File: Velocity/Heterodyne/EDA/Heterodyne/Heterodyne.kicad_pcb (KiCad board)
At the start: 2 copper layers, 59 x 44 mm, 31 parts, among them J3 PWR, J4 Doppler_Out, J5 V_Square, J6 OP_OUT, J7 Reciever, J8 Emmiter, U1 SA612AD, U2 NE5532, U3 MAX7375AXR105

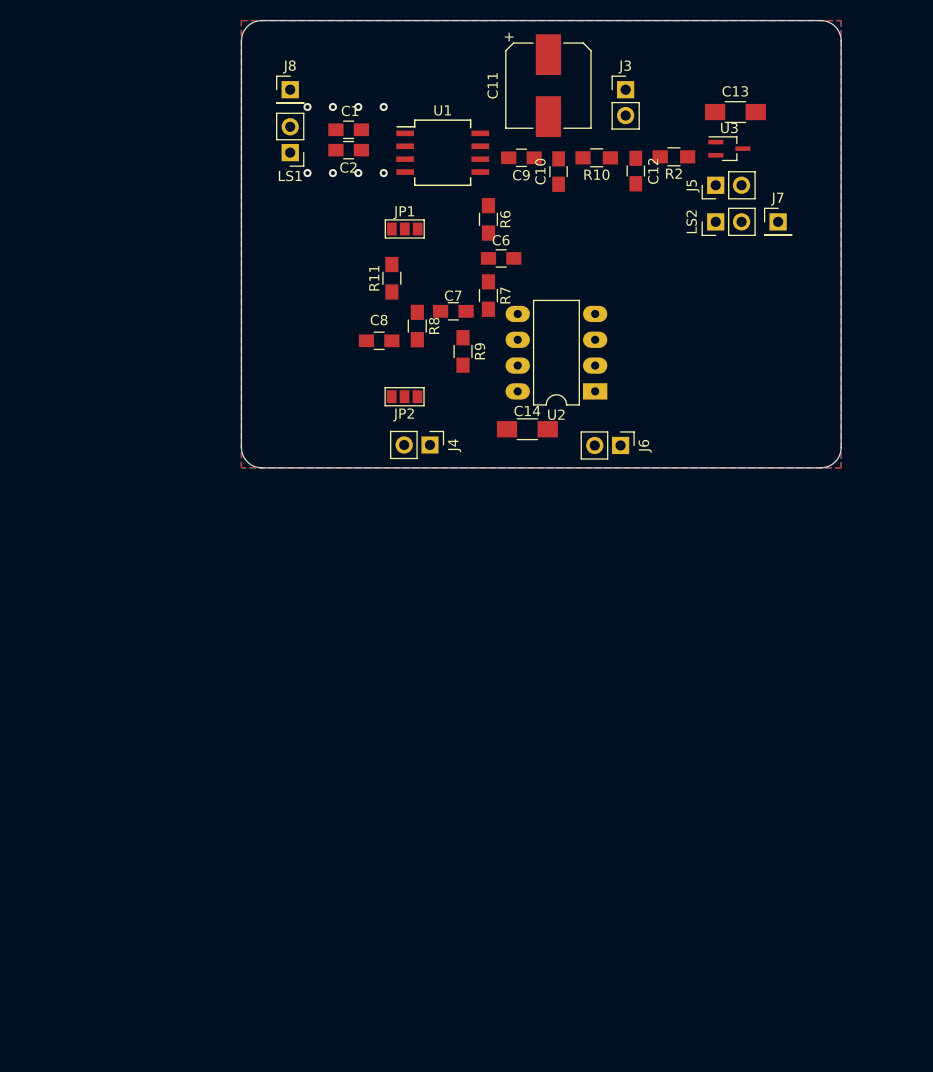
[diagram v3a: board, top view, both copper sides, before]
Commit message: updated data to heterodyne pcb to include adc
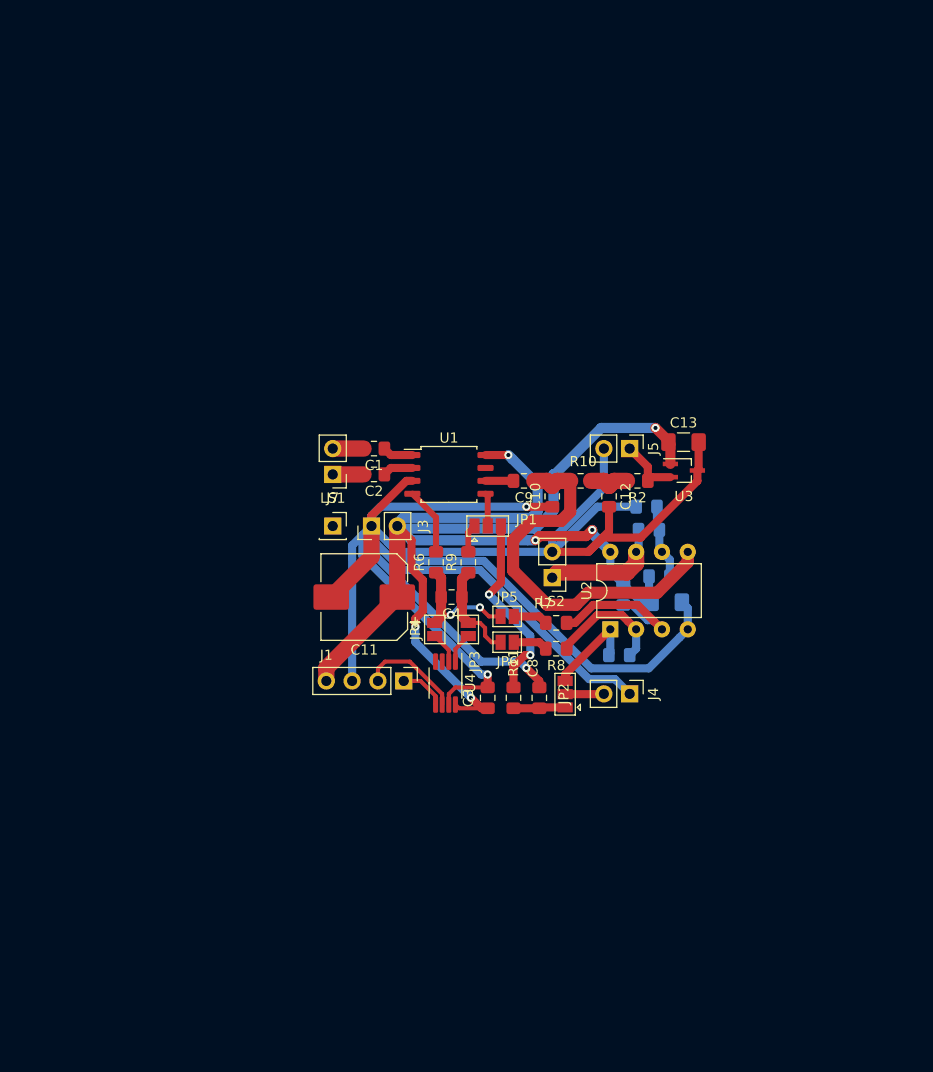
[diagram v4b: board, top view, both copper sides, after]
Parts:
- removed C6, C7: 100 nF, Capacitors_SMD:C_0805_HandSoldering
- removed J6: OP_OUT, Pin_Headers:Pin_Header_Straight_1x02_Pitch2.54mm
- removed J8: Emmiter, Pin_Headers:Pin_Header_Straight_1x01_Pitch2.54mm
- added C3: 100 nF, Capacitor_SMD:C_0805_2012Metric_Pad1.15x1.40mm_HandSolder, F.Cu at (149.2, 102.6)
- added C4: 22 nF, Capacitor_SMD:C_0805_2012Metric_Pad1.15x1.40mm_HandSolder, F.Cu at (145.7, 92.7)
- added J1: I2C, Connector_PinHeader_2.54mm:PinHeader_1x04_P2.54mm_Vertical, F.Cu at (141.0, 101.0)
- added JP3: SolderJumper_2_Open, Jumper:SolderJumper-2_P1.3mm_Open_Pad1.0x1.5mm, F.Cu at (147.3, 95.9)
- added JP4: SolderJumper_2_Open, Jumper:SolderJumper-2_P1.3mm_Open_Pad1.0x1.5mm, F.Cu at (144.0, 95.9)
- added JP5: SolderJumper_2_Open, Jumper:SolderJumper-2_P1.3mm_Open_Pad1.0x1.5mm, F.Cu at (151.1, 94.6)
- added JP6: SolderJumper_2_Open, Jumper:SolderJumper-2_P1.3mm_Open_Pad1.0x1.5mm, F.Cu at (151.1, 97.2)
- added R1: 1 kΩ, Resistor_SMD:R_0805_2012Metric_Pad1.15x1.40mm_HandSolder, B.Cu at (166.1, 90.7)
- added R12: 18 kΩ, Resistor_SMD:R_0805_2012Metric_Pad1.15x1.40mm_HandSolder, B.Cu at (162.2, 98.4)
- added R3: 1 kΩ, Resistor_SMD:R_0805_2012Metric_Pad1.15x1.40mm_HandSolder, B.Cu at (164.9, 83.8)
- added R4: 39 kΩ, Resistor_SMD:R_0805_2012Metric_Pad1.15x1.40mm_HandSolder, B.Cu at (165.1, 86.1)
- added R5: 18 kΩ, Resistor_SMD:R_0805_2012Metric_Pad1.15x1.40mm_HandSolder, B.Cu at (162.6, 92.5)
- added U4: MAX11613, Package_SO:MSOP-8_3x3mm_P0.65mm, F.Cu at (145.1, 101.2)
- C1, C10, C12, C2, C9: footprint Capacitors_SMD:C_0805_HandSoldering -> Capacitor_SMD:C_0805_2012Metric_Pad1.15x1.40mm_HandSolder
- C11: footprint Capacitors_SMD:CP_Elec_8x10 -> Capacitor_SMD:CP_Elec_8x10
- C13: footprint Capacitors_SMD:C_1206_HandSoldering -> Capacitor_SMD:C_1206_3216Metric_Pad1.42x1.75mm_HandSolder
- C14: footprint Capacitors_SMD:C_1206_HandSoldering -> Capacitor_SMD:C_1206_3216Metric_Pad1.42x1.75mm_HandSolder; moved to B.Cu
- C8: value 100 nF -> 22 nF; footprint Capacitors_SMD:C_0805_HandSoldering -> Capacitor_SMD:C_0805_2012Metric_Pad1.15x1.40mm_HandSolder
- J3, J4, J5, LS1, LS2: footprint Pin_Headers:Pin_Header_Straight_1x02_Pitch2.54mm -> Connector_PinHeader_2.54mm:PinHeader_1x02_P2.54mm_Vertical
- J7: footprint Pin_Headers:Pin_Header_Straight_1x01_Pitch2.54mm -> Connector_PinSocket_2.54mm:PinSocket_1x01_P2.54mm_Vertical
- JP1, JP2: footprint Connectors:GS3 -> Jumper:SolderJumper-3_P1.3mm_Open_Pad1.0x1.5mm
- R10, R11, R2: footprint Resistors_SMD:R_0805_HandSoldering -> Resistor_SMD:R_0805_2012Metric_Pad1.15x1.40mm_HandSolder
- R6: value 10 kΩ -> 330 Ω; footprint Resistors_SMD:R_0805_HandSoldering -> Resistor_SMD:R_0805_2012Metric_Pad1.15x1.40mm_HandSolder
- R7, R8: value 10 kΩ -> 1 kΩ; footprint Resistors_SMD:R_0805_HandSoldering -> Resistor_SMD:R_0805_2012Metric_Pad1.15x1.40mm_HandSolder
- R9: value 39 kΩ -> 330 Ω; footprint Resistors_SMD:R_0805_HandSoldering -> Resistor_SMD:R_0805_2012Metric_Pad1.15x1.40mm_HandSolder
- U1: footprint Housings_SOIC:SO-8_5.3x6.2mm_Pitch1.27mm -> Package_SO:SOIC-8_5.275x5.275mm_P1.27mm
- U2: footprint Housings_DIP:DIP-8_W7.62mm_LongPads -> Package_DIP:DIP-8_W7.62mm
- U3: footprint TO_SOT_Packages_SMD:SOT-323_SC-70_Handsoldering -> Package_TO_SOT_SMD:SOT-323_SC-70_Handsoldering
- moved C11 53.5 mm to (137.1, 92.7), turned to 180 degrees
- moved J7 53.1 mm to (134.0, 85.7)
- moved J3 49.7 mm to (137.8, 85.7), turned to 90 degrees
- moved R11 43.0 mm to (151.8, 102.6)
- moved LS2 38.5 mm to (155.6, 90.8), turned to 180 degrees
- moved C8 38.5 mm to (154.3, 102.6), turned to 90 degrees
- moved R8 34.6 mm to (156.0, 97.8), turned to 180 degrees
- moved R6 34.1 mm to (144.1, 89.3), turned to 90 degrees
- moved JP2 33.3 mm to (156.8, 102.3)
- moved R7 32.9 mm to (156.0, 95.2), turned to 180 degrees
- moved C13 32.9 mm to (168.5, 77.5)
- moved C12 32.1 mm to (161.2, 82.8)
- moved R2 32.1 mm to (164.0, 81.3)
- moved C2 32.0 mm to (138.0, 80.6)
- moved U3 32.0 mm to (168.5, 80.3)
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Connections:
- JP1 pad 1: Net-(C7-Pad2) -> Net-(JP1-Pad1)
- JP2 pad 3: Net-(C6-Pad2) -> Net-(JP2-Pad3)
- LS2 pad 1: Net-(J5-Pad1) -> Net-(LS2-Pad1)
- R6 pad 1: Net-(R6-Pad1) -> Net-(C4-Pad2)
- R6 pad 2: Net-(C6-Pad1) -> Net-(R6-Pad2)
- R7 pad 1: Net-(C6-Pad1) -> Net-(R5-Pad1)
- R7 pad 2: Net-(C7-Pad1) -> Net-(JP5-Pad2)
- R8 pad 1: Net-(C7-Pad2) -> Net-(R12-Pad1)
- R8 pad 2: Net-(R8-Pad2) -> Net-(JP6-Pad2)
- R9 pad 1: Net-(R8-Pad2) -> Net-(C4-Pad1)
- R9 pad 2: Net-(C6-Pad2) -> Net-(JP1-Pad1)
- U1 pad 4: Net-(JP1-Pad2) -> Net-(R6-Pad2)
- U1 pad 5: Net-(R6-Pad1) -> Net-(JP1-Pad2)
- U2 pad 1: Net-(J6-Pad2) -> Net-(JP2-Pad3)
- U2 pad 2: Net-(R1-Pad2) -> Net-(R12-Pad1)
- U2 pad 3: Driver_Wave -> Net-(R5-Pad1)
- U2 pad 5: Net-(C7-Pad1) -> Driver_Wave
- U2 pad 6: Net-(R8-Pad2) -> Net-(R1-Pad2)
- U2 pad 7: Net-(C6-Pad2) -> Net-(LS2-Pad1)
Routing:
- net GND: track 0.00 -> 240.8 mm, vias 8 -> 3
- net VPP: track 0.00 -> 136.4 mm, vias 0 -> 6
- net Driver_Wave: track 0.00 -> 38.1 mm
- net Net-(JP1-Pad3): track 0.00 -> 19.0 mm, vias 0 -> 2
- net Net-(R5-Pad1): track 0.00 -> 15.9 mm
- net Net-(LS2-Pad1): track 0.00 -> 12.2 mm
- net Net-(C4-Pad2): track 0.00 -> 12.0 mm, vias 0 -> 2
- net Net-(R12-Pad1): track 0.00 -> 11.8 mm
- net Net-(J1-Pad2): track 0.00 -> 10.2 mm
- net Net-(C4-Pad1): track 0.00 -> 9.87 mm
- net Net-(JP2-Pad3): track 0.00 -> 9.52 mm
- net Net-(R1-Pad2): track 0.00 -> 7.38 mm
- net Net-(R6-Pad2): track 0.00 -> 6.68 mm
- net Net-(J5-Pad1): track 0.00 -> 6.28 mm
- net Net-(C8-Pad1): track 0.00 -> 5.12 mm
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- removed copper zone on B.Cu, net GND
- removed copper zone on F.Cu, net GND
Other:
- board outline removed

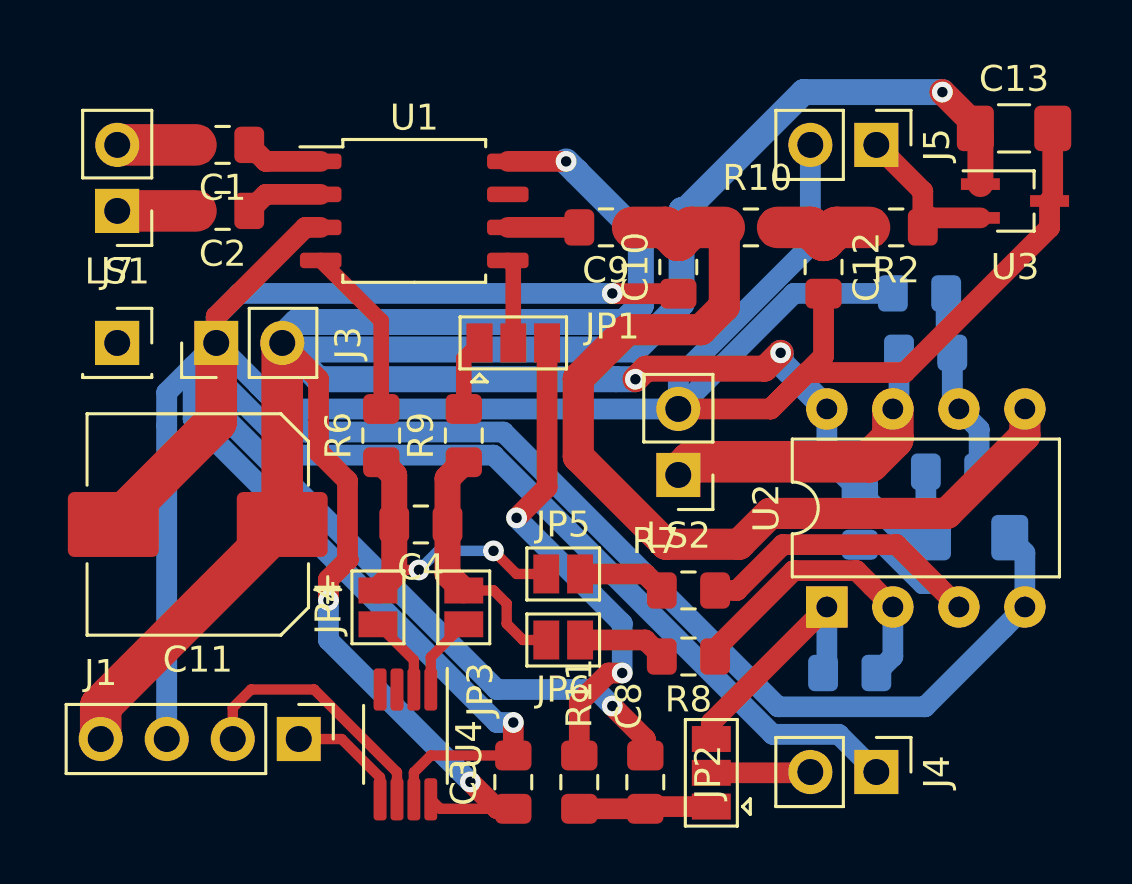
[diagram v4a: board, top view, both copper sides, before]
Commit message: finshsed routing 2 layer board
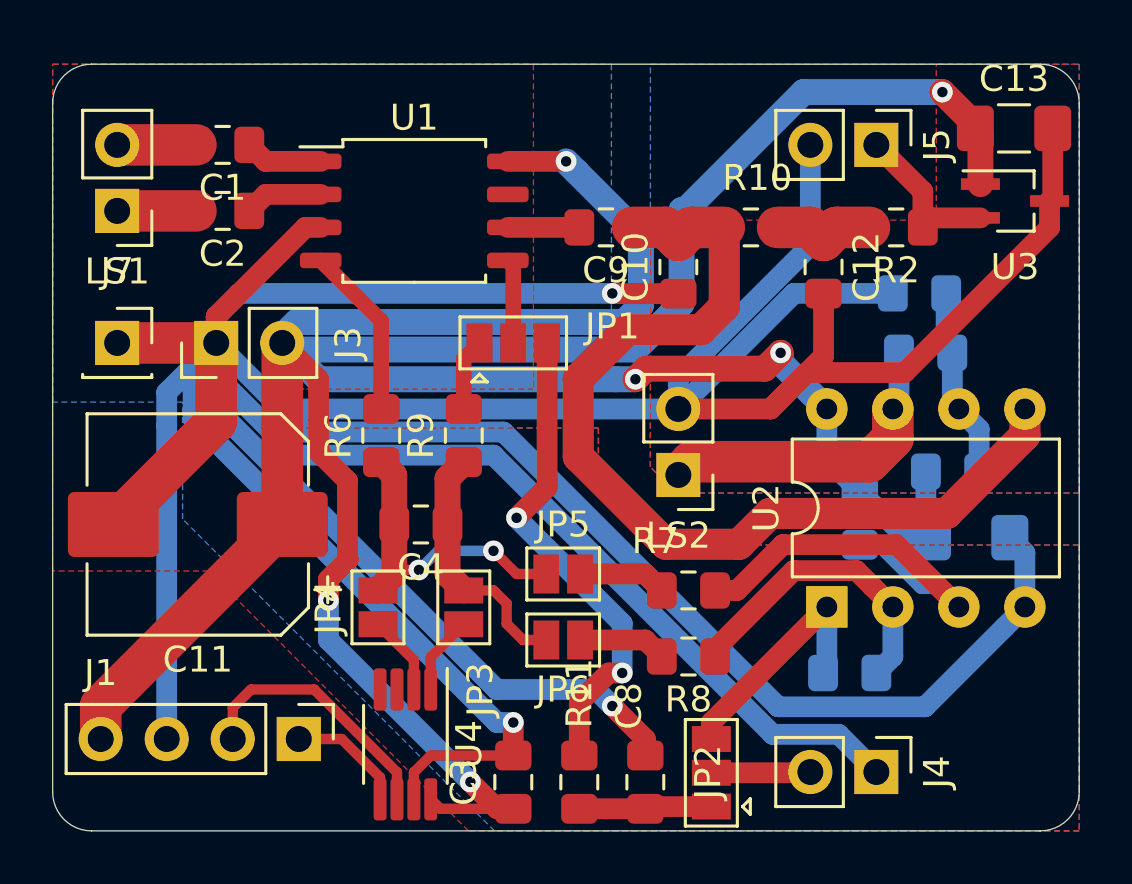
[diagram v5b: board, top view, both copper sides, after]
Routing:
- net GND: track 240.8 -> 244.6 mm
- added copper zone on B.Cu, net GND
- added copper zone on F.Cu, net GND
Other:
- board outline added: 39.5 x 29.5 mm

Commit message: calibrated velocity, implemented multi sample rate rangeing
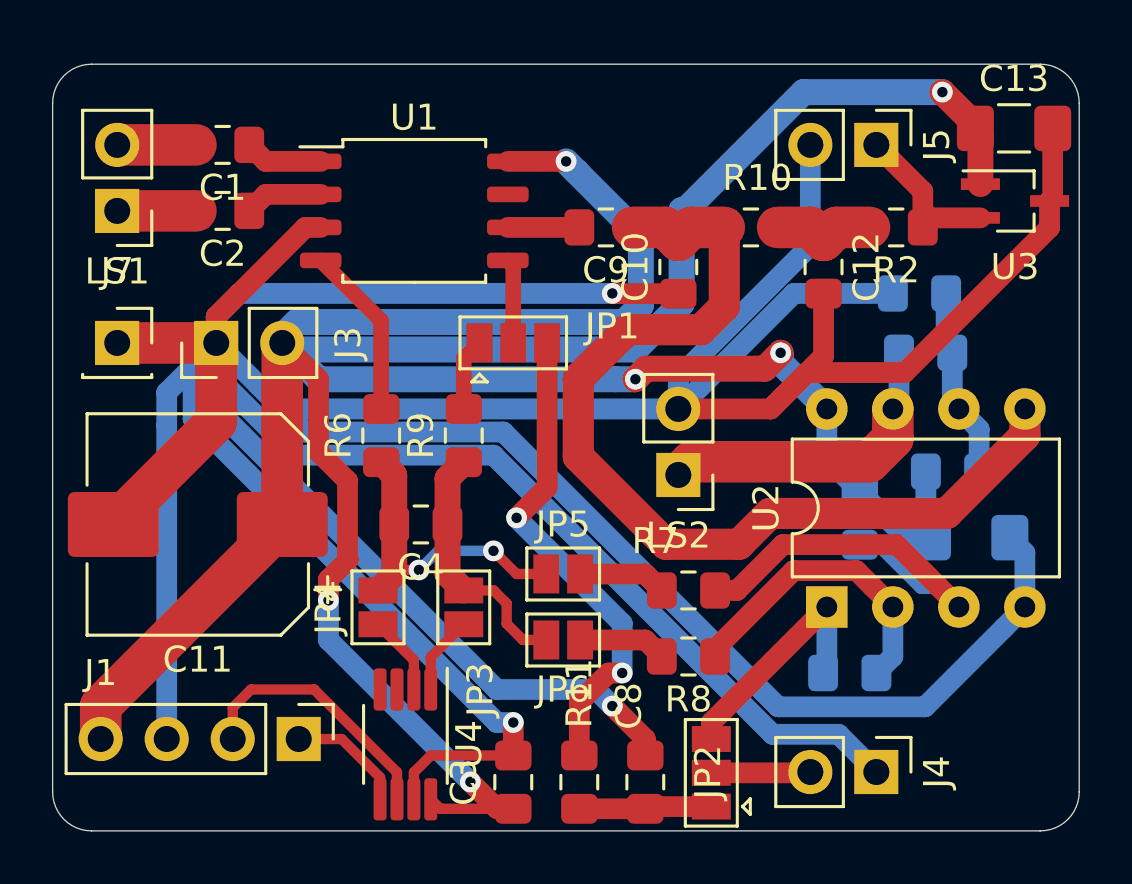
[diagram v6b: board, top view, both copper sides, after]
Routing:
- removed copper zone on B.Cu, net GND
- removed copper zone on F.Cu, net GND
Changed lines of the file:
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@@
   (segment (start 156.845 100.33) (end 161.29 95.885) (width 0.8) (layer F.Cu) (net 32) (status 20))
   (segment (start 156.845 100.965) (end 156.845 100.33) (width 0.8) (layer F.Cu) (net 32) (status 10))
-  (zone (net 1) (net_name GND) (layer B.Cu) (hatch edge 0.508)
-    (connect_pads (clearance 0.508))
-    (min_thickness 0.254)
-    (fill yes (arc_segments 32) (thermal_gap 0.508) (thermal_bridge_width 0.508) (smoothing fillet) (radius 1))
-    (polygon
-      (pts
-        (xy 153 87.5) (xy 140.5 87.5) (xy 140.5 89) (xy 152.5 89) (xy 152.5 91.5)
-        (xy 154.5 93.5) (xy 171 93.5) (xy 171 104.5) (xy 148.5 104.5) (xy 143 99)
-        (xy 136.5 92.5) (xy 136.5 88) (xy 131.5 88) (xy 131.5 75) (xy 153 75)
-      )
-    )
-  )
-  (zone (net 1) (net_name GND) (layer B.Cu) (hatch edge 0.508)
-    (connect_pads (clearance 0.508))
-    (min_thickness 0.254)
-    (fill yes (arc_segments 32) (thermal_gap 0.508) (thermal_bridge_width 0.508) (smoothing fillet) (radius 1))
-    (polygon
-      (pts
-        (xy 171 91.5) (xy 155.5 91.5) (xy 154.5 90.5) (xy 154.5 75) (xy 171 75)
-      )
-    )
-  )
-  (zone (net 1) (net_name GND) (layer F.Cu) (hatch edge 0.508)
-    (connect_pads (clearance 0.508))
-    (min_thickness 0.254)
-    (fill yes (arc_segments 32) (thermal_gap 0.508) (thermal_bridge_width 0.508) (smoothing fillet) (radius 1))
-    (polygon
-      (pts
-        (xy 150 87.5) (xy 140.5 87.5) (xy 140.5 89) (xy 152.5 89) (xy 152.5 91.5)
-        (xy 154.5 93.5) (xy 171 93.5) (xy 171 104.5) (xy 148.5 104.5) (xy 147.5 104.5)
-        (xy 137.5 94.5) (xy 131.5 94.5) (xy 131.5 88) (xy 131.5 75) (xy 150 75)
-      )
-    )
-  )
-  (zone (net 1) (net_name GND) (layer F.Cu) (hatch edge 0.508)
-    (connect_pads (clearance 0.508))
-    (min_thickness 0.254)
-    (fill yes (arc_segments 32) (thermal_gap 0.508) (thermal_bridge_width 0.508) (smoothing fillet) (radius 1))
-    (polygon
-      (pts
-        (xy 171 91.5) (xy 155.5 91.5) (xy 154.5 90.5) (xy 154.5 81) (xy 165.5 81)
-        (xy 165.5 75) (xy 171 75)
-      )
-    )
-  )
 )
